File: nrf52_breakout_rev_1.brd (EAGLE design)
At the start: 38.8 x 25.5 mm, 23 parts, among them IC1 E73_2G4M04S

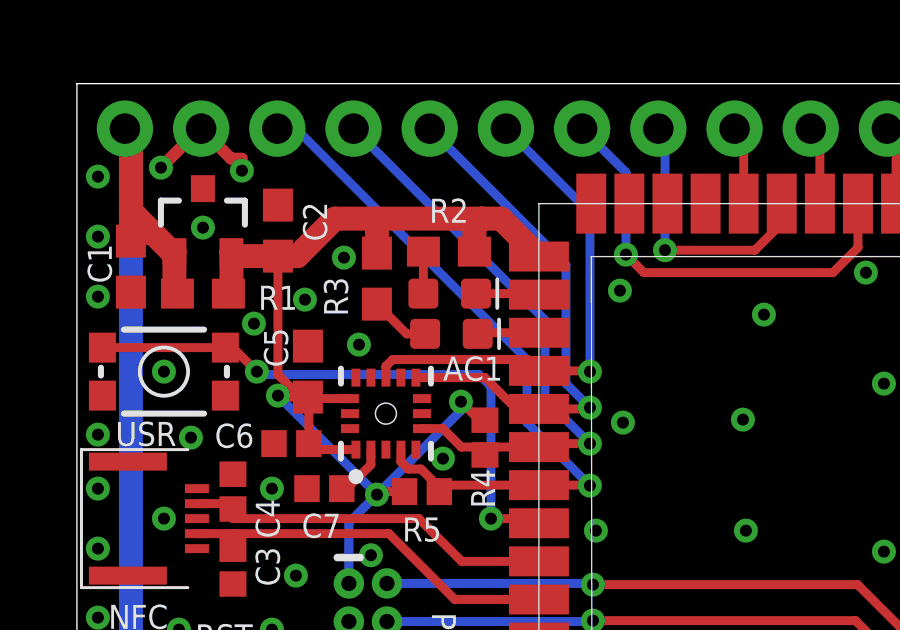
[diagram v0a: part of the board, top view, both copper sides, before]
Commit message: added some stuff to the silkscreen
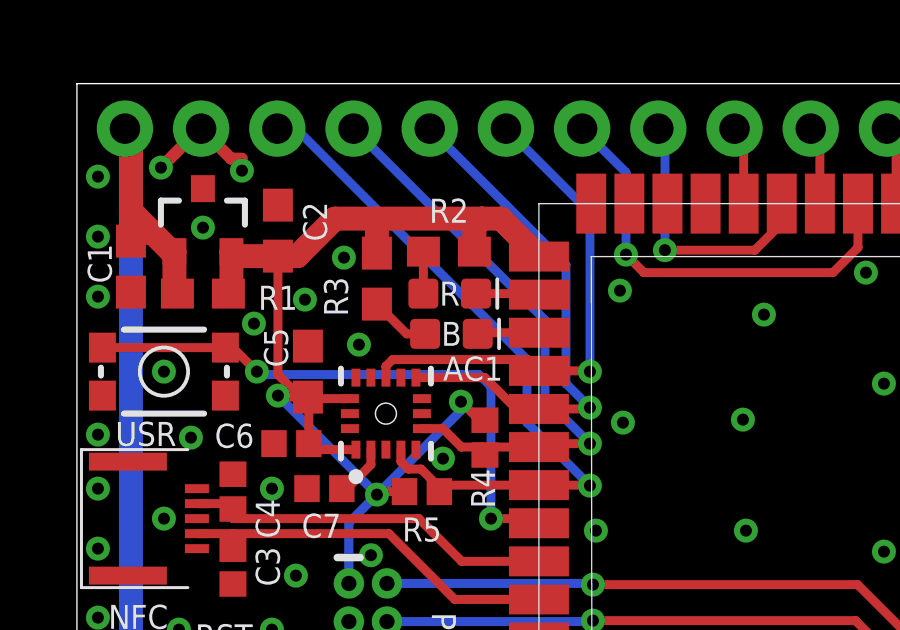
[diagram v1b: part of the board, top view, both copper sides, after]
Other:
- board text added: "B"
- board text added: "R"
- board text added: "X"
- board text added: "Y"
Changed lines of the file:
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@@
 <wire x1="27" y1="19" x2="37" y2="19" width="0.2" layer="22"/>
 <wire x1="37" y1="19" x2="37" y2="6.5" width="0.2" layer="22"/>
+<wire x1="20.119125" y1="9.84125" x2="20.119125" y2="11.48425" width="0.254" layer="22"/>
+<wire x1="20.119125" y1="9.84125" x2="20.373125" y2="10.09525" width="0.254" layer="22"/>
+<wire x1="20.119125" y1="9.84125" x2="19.865125" y2="10.09525" width="0.254" layer="22"/>
+<wire x1="20.398525" y1="10.12065" x2="19.839725" y2="10.12065" width="0.254" layer="22"/>
+<text x="21.4682" y="13.439725" size="1.016" layer="22" font="vector" ratio="15" rot="SR270">Y</text>
+<text x="18.60775" y="11.456975" size="1.016" layer="22" font="vector" ratio="15" rot="SR270">X</text>
+<wire x1="22.45415" y1="12.129925" x2="20.81115" y2="12.129925" width="0.254" layer="22"/>
+<wire x1="22.45415" y1="12.129925" x2="22.20015" y2="12.383925" width="0.254" layer="22"/>
+<wire x1="22.45415" y1="12.129925" x2="22.20015" y2="11.875925" width="0.254" layer="22"/>
+<wire x1="22.17475" y1="12.409325" x2="22.17475" y2="11.850525" width="0.254" layer="22"/>
+<text x="12.4242625" y="18.499996875" size="0.8" layer="25" ratio="13" align="center">R</text>
+<text x="12.48284375" y="17.15856875" size="0.8" layer="25" ratio="13" align="center">B</text>
 </plain>
 <attributes>
